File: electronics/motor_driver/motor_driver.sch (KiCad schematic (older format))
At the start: 72 parts, among them J1 Power, J2 Control, J3 Motor, Q1 FDD86381, Q2 FDD86381, Q3 FDD86381, Q4 FDD86381, U1 SY8502, U2 L78L05_SOT89, U3 LTV-356T, U4 TLP2270, U5 L6393, U6 L6393, U7 LTV-356T

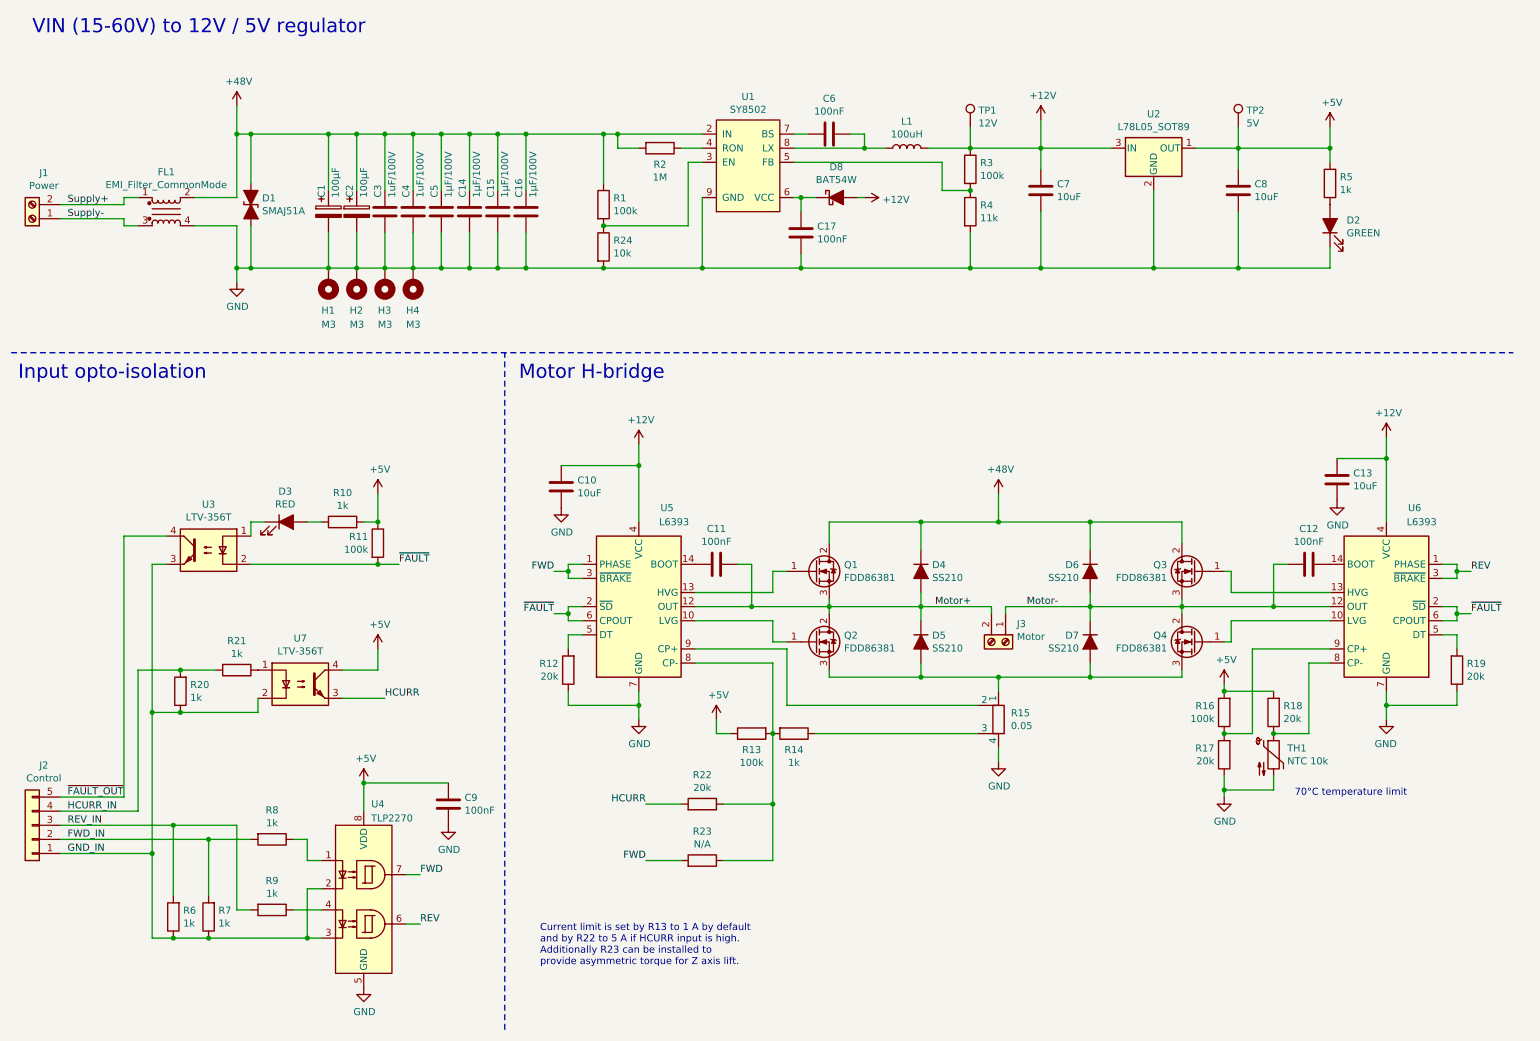
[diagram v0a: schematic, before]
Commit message: Update motor driver and power control PCB designs
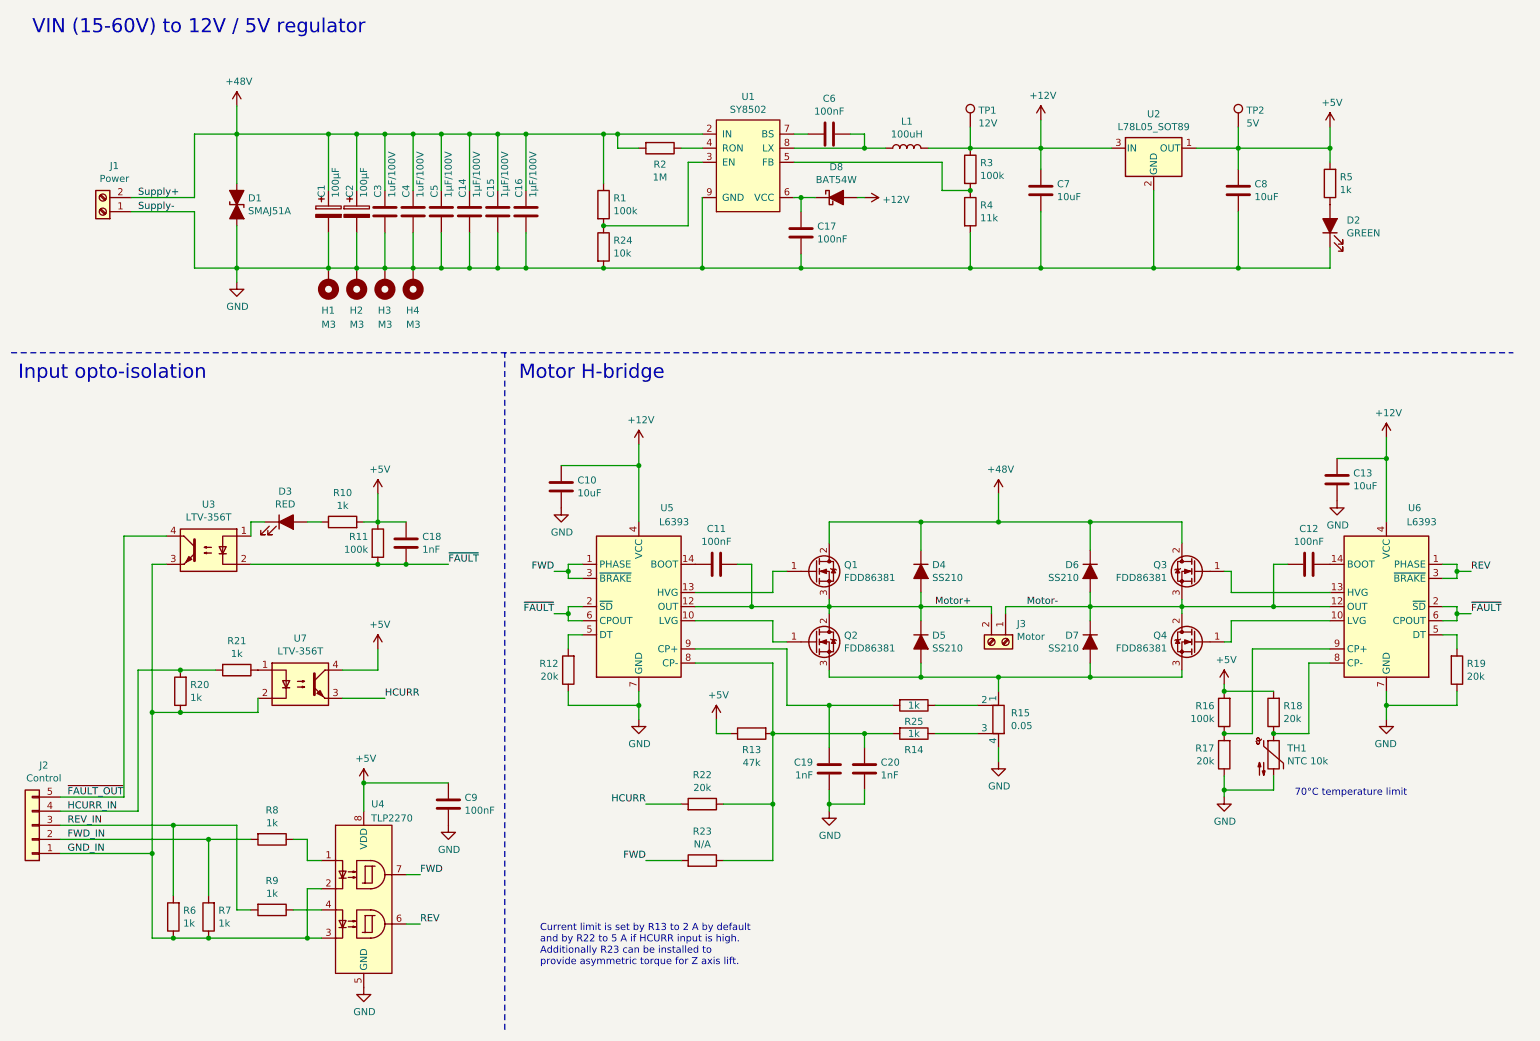
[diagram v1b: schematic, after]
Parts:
- removed FL1: EMI_Filter_CommonMode, motor_driver:CM7060, symbol Device:EMI_Filter_CommonMode
- added C18, C19, C20: 1nF, Capacitor_SMD:C_0603_1608Metric, symbol Device:C
- added R25: 1k, Resistor_SMD:R_0603_1608Metric, symbol Device:R
- R13: value 100k -> 47k
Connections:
- net Supply+ is gone; now on net +48V: J1.2 (Pin_2)
- net Supply- is gone; now on net GND: J1.1 (Pin_1)
- net +5V: now also C18.1
- net GND: now also C19.2, C20.2
- net ~FAULT: now also C18.2
- net at R15.2: now also R25.1; no longer U5.9 (CP+)
- net at R13.2, R14.2, R22.1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: now also C20.1
- new net: C19.1, R25.2, U5.9 (CP+)
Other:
- note added: "Current limit is set by R13 to 2 A by default\nand by R22 to 5 A if HCURR input is high.\nAdditionally R23 can be installed to\nprovide asymmetric torque for Z axis lift."
- note removed: "Current limit is set by R13 to 1 A by default\nand by R22 to 5 A if HCURR input is high.\nAdditionally R23 can be installed to\nprovide asymmetric torque for Z axis lift."
- moved on the sheet: D1, J1, R14
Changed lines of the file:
@@
 L Connector:Screw_Terminal_01x02 J1
 U 1 1 61887827
-P 650 2000
-F 0 "J1" H 568 1675 50  0000 C CNN
-F 1 "Power" H 568 1766 50  0000 C CNN
-F 2 "TerminalBlock:TerminalBlock_bornier-2_P5.08mm" H 650 2000 50  0001 C CNN
-F 3 "~" H 650 2000 50  0001 C CNN
-	1    650  2000
+P 1150 1950
+F 0 "J1" H 1068 1625 50  0000 C CNN
+F 1 "Power" H 1068 1716 50  0000 C CNN
+F 2 "TerminalBlock:TerminalBlock_bornier-2_P5.08mm" H 1150 1950 50  0001 C CNN
+F 3 "~" H 1150 1950 50  0001 C CNN
+	1    1150 1950
 	-1   0    0    1
 $EndComp
-$Comp
-L Device:EMI_Filter_CommonMode FL1
-U 1 1 61888648
-P 1600 1950
-F 0 "FL1" H 1600 2231 50  0000 C CNN
-F 1 "EMI_Filter_CommonMode" H 1600 2140 50  0000 C CNN
-F 2 "motor_driver:CM7060" H 1600 1990 50  0001 C CNN
-F 3 "~" H 1600 1990 50  0001 C CNN
-	1    1600 1950
-	1    0    0    -1
-$EndComp
-Wire Wire Line
-	1400 1850 1300 1850
-Wire Wire Line
-	1300 1850 1300 1900
-Wire Wire Line
-	1300 1900 850  1900
-Wire Wire Line
-	850  2000 1300 2000
-Wire Wire Line
-	1300 2000 1300 2050
-Wire Wire Line
-	1300 2050 1400 2050
+Wire Wire Line
+	1800 1850 1350 1850
+Wire Wire Line
+	1350 1950 1800 1950
 $Comp
 L Device:CP C1
@@
 	7500 5850 7500 5750
 Wire Wire Line
-	7350 5450 6000 5450
-Wire Wire Line
 	6000 5450 6000 5050
 Wire Wire Line
@@
 P 5750 5650
 F 0 "R13" V 5865 5650 50  0000 C CNN
-F 1 "100k" V 5956 5650 50  0000 C CNN
+F 1 "47k" V 5956 5650 50  0000 C CNN
 F 2 "Resistor_SMD:R_0603_1608Metric" V 5680 5650 50  0001 C CNN
 F 3 "~" H 5750 5650 50  0001 C CNN
@@
 L Device:R R14
 U 1 1 61931B2A
-P 6050 5650
-F 0 "R14" V 6165 5650 50  0000 C CNN
-F 1 "1k" V 6256 5650 50  0000 C CNN
-F 2 "Resistor_SMD:R_0603_1608Metric" V 5980 5650 50  0001 C CNN
-F 3 "~" H 6050 5650 50  0001 C CNN
-	1    6050 5650
+P 6900 5650
+F 0 "R14" V 7015 5650 50  0000 C CNN
+F 1 "1k" V 6900 5650 50  0000 C CNN
+F 2 "Resistor_SMD:R_0603_1608Metric" V 6830 5650 50  0001 C CNN
+F 3 "~" H 6900 5650 50  0001 C CNN
+	1    6900 5650
 	0    1    1    0
 $EndComp
-Wire Wire Line
-	6200 5650 7350 5650
 Wire Wire Line
 	5900 5650 5900 5150
@@
 	2750 2350 2950 2350
 Connection ~ 2950 2350
-Wire Wire Line
-	1800 1850 2100 1850
-Wire Wire Line
-	1800 2050 2100 2050
-Wire Wire Line
-	2100 2050 2100 2350
-Wire Wire Line
-	2100 2350 2200 2350
 Connection ~ 2750 2350
 Wire Wire Line
 	2100 2450 2100 2350
-Connection ~ 2100 2350
 $Comp
 L Device:C C6
@@
 	0    -1   -1   0
 $EndComp
-Text Label 3250 4450 0    50   ~ 0
+Text Label 3600 4450 0    50   ~ 0
 ~FAULT
 $Comp
@@
 $EndComp
 Connection ~ 3350 2350
-Connection ~ 2100 1400
 Wire Wire Line
 	2100 1200 2100 1400
 Connection ~ 2750 1400
-Wire Wire Line
-	2100 1400 2200 1400
-Wire Wire Line
-	2100 1850 2100 1400
 Connection ~ 2950 1400
 Wire Wire Line
@@
 	-1   0    0    1
 $EndComp
-Text Label 900  1900 0    50   ~ 0
+Text Label 1400 1850 0    50   ~ 0
 Supply+
-Text Label 900  2000 0    50   ~ 0
+Text Label 1400 1950 0    50   ~ 0
 Supply-
 $Comp
@@
 Connection ~ 3100 4450
 Wire Wire Line
-	3100 4450 3250 4450
+	3100 4450 3300 4450
 Wire Wire Line
 	2200 4250 2200 4150
@@
 70°C temperature limit
 Text Notes 4250 7300 0    50   ~ 0
-Current limit is set by R13 to 1 A by default\nand by R22 to 5 A if HCURR input is high.\nAdditionally R23 can be installed to\nprovide asymmetric torque for Z axis lift.
+Current limit is set by R13 to 2 A by default\nand by R22 to 5 A if HCURR input is high.\nAdditionally R23 can be installed to\nprovide asymmetric torque for Z axis lift.
 $Comp
 L Device:R R20
@@
 L Device:D_TVS_ALT D1
 U 1 1 6285B635
-P 2200 1900
-F 0 "D1" V 2154 1980 50  0000 L CNN
-F 1 "SMAJ51A" V 2245 1980 50  0000 L CNN
-F 2 "Diode_SMD:D_SMA" H 2200 1900 50  0001 C CNN
-F 3 "~" H 2200 1900 50  0001 C CNN
-	1    2200 1900
+P 2100 1900
+F 0 "D1" V 2054 1980 50  0000 L CNN
+F 1 "SMAJ51A" V 2145 1980 50  0000 L CNN
+F 2 "Diode_SMD:D_SMA" H 2100 1900 50  0001 C CNN
+F 3 "~" H 2100 1900 50  0001 C CNN
+	1    2100 1900
 	0    1    1    0
 $EndComp
 Wire Wire Line
-	2200 2050 2200 2350
-Connection ~ 2200 2350
-Wire Wire Line
-	2200 2350 2750 2350
-Wire Wire Line
-	2200 1750 2200 1400
-Connection ~ 2200 1400
-Wire Wire Line
-	2200 1400 2750 1400
+	2100 2050 2100 2350
+Wire Wire Line
+	2100 1750 2100 1400
 Wire Wire Line
 	3350 2100 3350 2350
@@
 Wire Wire Line
 	4150 2350 4700 2350
+$Comp
+L Device:C C18
+U 1 1 61C9C9BC
+P 3300 4300
+F 0 "C18" H 3415 4346 50  0000 L CNN
+F 1 "1nF" H 3415 4255 50  0000 L CNN
+F 2 "Capacitor_SMD:C_0603_1608Metric" H 3338 4150 50  0001 C CNN
+F 3 "~" H 3300 4300 50  0001 C CNN
+	1    3300 4300
+	1    0    0    -1
+$EndComp
+Connection ~ 3300 4450
+Wire Wire Line
+	3300 4450 3600 4450
+Wire Wire Line
+	3300 4150 3100 4150
+Wire Wire Line
+	7050 5650 7350 5650
+$Comp
+L Device:R R25
+U 1 1 61CC7027
+P 6900 5450
+F 0 "R25" V 7015 5450 50  0000 C CNN
+F 1 "1k" V 6900 5450 50  0000 C CNN
+F 2 "Resistor_SMD:R_0603_1608Metric" V 6830 5450 50  0001 C CNN
+F 3 "~" H 6900 5450 50  0001 C CNN
+	1    6900 5450
+	0    1    1    0
+$EndComp
+Wire Wire Line
+	7050 5450 7350 5450
+Wire Wire Line
+	6750 5650 6550 5650
+Wire Wire Line
+	6000 5450 6300 5450
+$Comp
+L Device:C C20
+U 1 1 61D06CBC
+P 6550 5900
+F 0 "C20" H 6665 5946 50  0000 L CNN
+F 1 "1nF" H 6665 5855 50  0000 L CNN
+F 2 "Capacitor_SMD:C_0603_1608Metric" H 6588 5750 50  0001 C CNN
+F 3 "~" H 6550 5900 50  0001 C CNN
+	1    6550 5900
+	1    0    0    -1
+$EndComp
+$Comp
+L Device:C C19
+U 1 1 61D073FF
+P 6300 5900
+F 0 "C19" H 6185 5946 50  0000 R CNN
+F 1 "1nF" H 6185 5855 50  0000 R CNN
+F 2 "Capacitor_SMD:C_0603_1608Metric" H 6338 5750 50  0001 C CNN
+F 3 "~" H 6300 5900 50  0001 C CNN
+	1    6300 5900
+	1    0    0    -1
+$EndComp
+$Comp
+L power:GND #PWR0102
+U 1 1 61D079EB
+P 6300 6200
+F 0 "#PWR0102" H 6300 5950 50  0001 C CNN
+F 1 "GND" H 6305 6027 50  0000 C CNN
+F 2 "" H 6300 6200 50  0001 C CNN
+F 3 "" H 6300 6200 50  0001 C CNN
+	1    6300 6200
+	1    0    0    -1
+$EndComp
+Wire Wire Line
+	6300 6200 6300 6150
+Wire Wire Line
+	6300 6150 6550 6150
+Wire Wire Line
+	6550 6150 6550 6050
+Connection ~ 6300 6150
+Wire Wire Line
+	6300 6150 6300 6050
+Wire Wire Line
+	6550 5750 6550 5650
+Connection ~ 6550 5650
+Wire Wire Line
+	6550 5650 5900 5650
+Wire Wire Line
+	6300 5750 6300 5450
+Connection ~ 6300 5450
+Wire Wire Line
+	6300 5450 6750 5450
+Wire Wire Line
+	2100 1400 1800 1400
+Wire Wire Line
+	1800 1400 1800 1850
+Connection ~ 2100 1400
+Wire Wire Line
+	1800 1950 1800 2350
+Wire Wire Line
+	1800 2350 2100 2350
+Connection ~ 2100 2350
+Wire Wire Line
+	2100 2350 2750 2350
+Wire Wire Line
+	2100 1400 2750 1400
 $EndSCHEMATC
